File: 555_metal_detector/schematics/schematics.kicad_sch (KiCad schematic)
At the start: 9 parts, among them J1 5V, U1 LM555xN

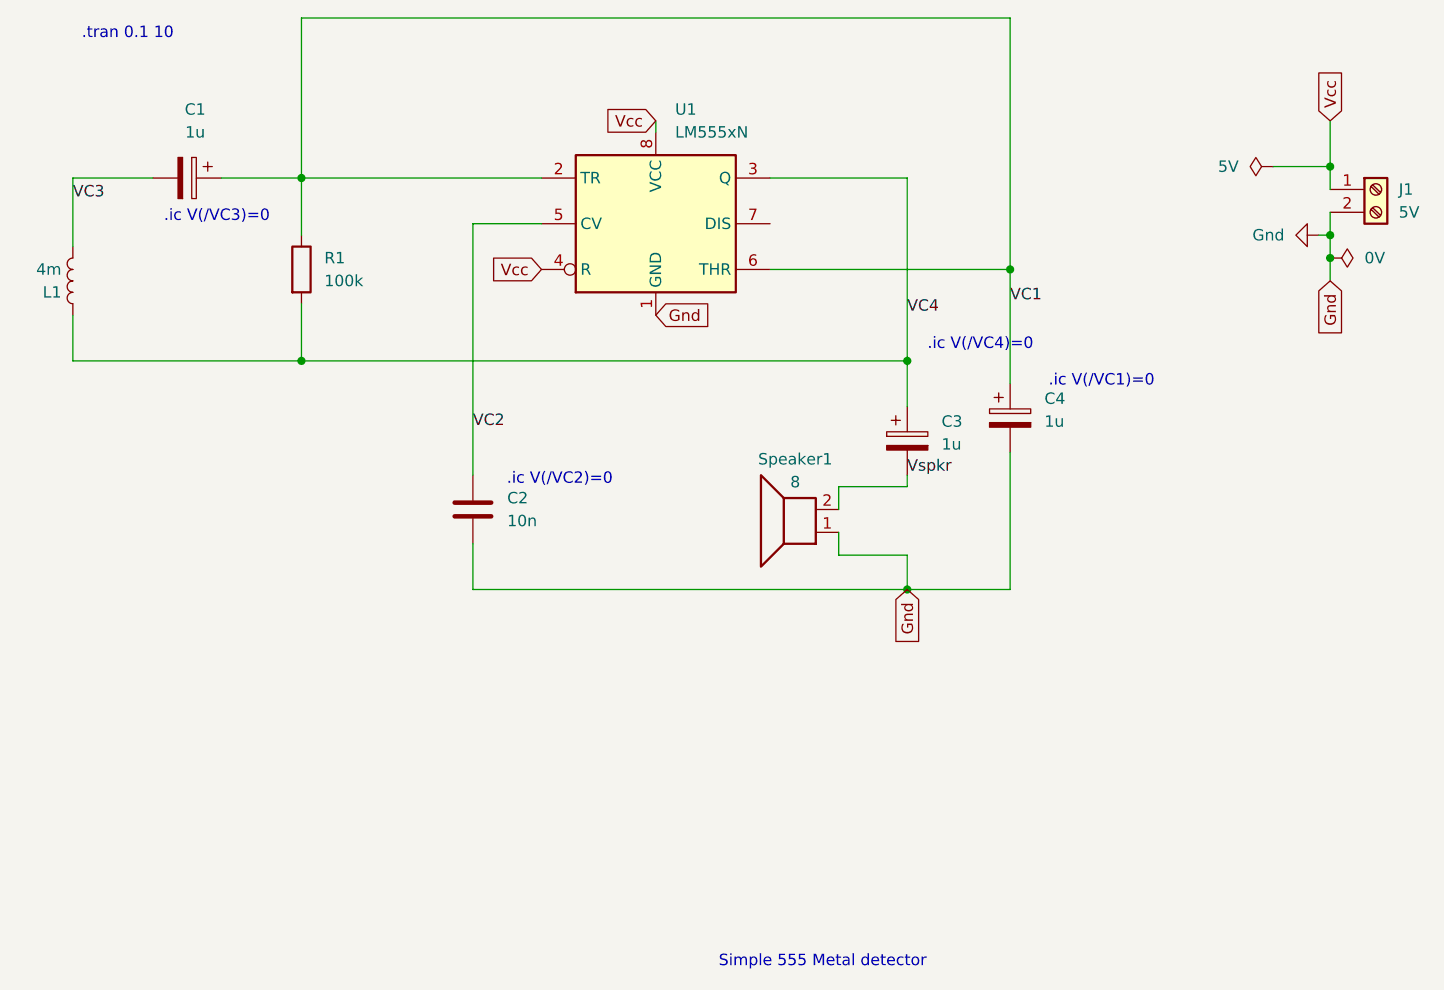
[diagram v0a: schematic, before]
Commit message: feat: Update 555_metal_detector documentation and schematics
Added oscilloscope images to practical analytics section.
Updated theoretical analytics workbook.
Included breadboard image for better visualization.
Revised schematics files for improved clarity and accuracy with new
values for components due to the fact that I was missing a few values.

Breaking changes: Changed values for components in schematics.

Resolves: None
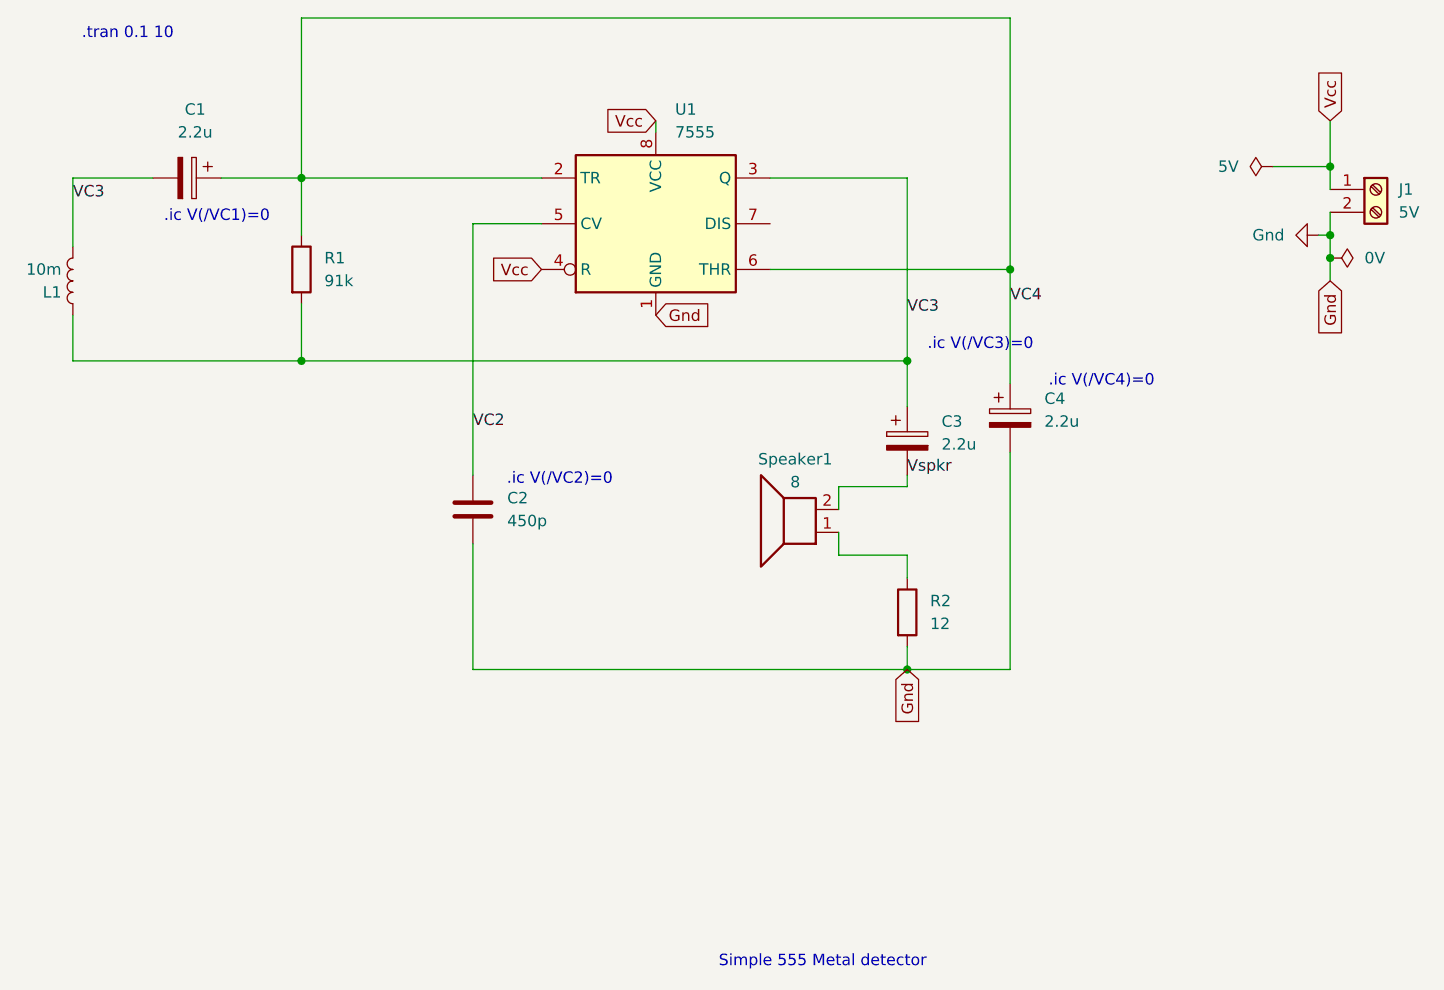
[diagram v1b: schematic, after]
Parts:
- added R2: 12, Resistor_THT:R_Axial_DIN0204_L3.6mm_D1.6mm_P2.54mm_Vertical, symbol Device:R
- C1, C3, C4: value 1u -> 2.2u
- C2: value 10n -> 450p
- L1: value 4m -> 10m
- R1: value 100k -> 91k
- U1: value LM555xN -> 7555
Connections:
- net VC1 is gone; now on net VC4: C1.1, C4.1, R1.1, U1.2 (TR), U1.6 (THR)
- net Gnd: now also R2.2; no longer Speaker1.1
- net VC3: now also C3.1, L1.1, R1.2, U1.3 (Q)
- net VC4: no longer C3.1, L1.1, R1.2, U1.3 (Q)
- new net: R2.1, Speaker1.1
